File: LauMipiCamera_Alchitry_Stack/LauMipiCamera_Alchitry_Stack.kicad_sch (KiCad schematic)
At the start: 19 parts, among them J1 DF40C-50DP, J2 DF40C-80DP, J3 DF40C-80DP, SW1 SW_DIP_x4

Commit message: hw(mipi): import netlist onto the PCB; repair what F8 broke
Update PCB from Schematic pulled all 23 nets onto the board: 268 pads netted,
0 node mismatches against the schematic netlist, and kicad-cli reports
schematic_parity: 0. The scaffold's R_1206 became R_0402 and the 9 XAPP894
front-end resistors were added. KiCad also annotated the non-numeric refs
(R_SCL -> R_SCL1, J_CAM -> J_CAM1, R_LP* -> R_LP*1); schematic and PCB agree.

F8 ran with "replace footprints", which re-created every footprint with new
UUIDs at default placement. Two consequences, both fixed here:

1. J1/J2/J3 landed on F.Cu. They are bottom-side DF40 plugs, and their old
   coordinates encoded the Alchitry stack geometry -- Site B-A = 21.5 mm in x,
   Site B-C = 37.0 mm in y (ROADMAP SS3, from Br.step). Restored all three to
   B.Cu at their original positions, injecting the freshly computed pad nets
   into the pre-F8 footprint blocks. Geometry re-verified: 21.50 / 37.00 mm.

2. Twelve clearance errors appeared, all pad-to-pad *inside* a single
   connector. Both causes are settings that were written before the nets
   existed, so nothing had ever exercised them:
     * "MipiHS clearance to other nets" (0.25 mm, ~3W) applied to pads as well
       as tracks. DF40 is 0.4 mm pitch and the FFC 0.5 mm -- those gaps are
       fixed by the connector and can never satisfy it. Scoped to
       A.Type == 'Track'; track-vs-pad is still checked.
     * The MipiHS netclass clearance floor was 0.2 mm vs the DF40's actual
       0.17 mm pad gap. Lowered to 0.15 mm; 3W routing separation still comes
       from the custom rule.

DRC now: 0 copper violations, schematic_parity 0. The 47 remaining are all
silkscreen overlaps from the auto-placement, and 112 unconnected ratsnest items
because nothing is routed.

Next: place the parts (front-end resistors belong at J3, not the FFC -- SS3.4),
then recompute the placeholder track width/gap from the real stackup.

Co-Authored-By: Claude Opus 4.8 (1M context) <nore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
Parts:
- renumbered J_CAM to J_CAM1, R_LP0N to R_LP0N1, R_LP0P to R_LP0P1, R_LP1N to R_LP1N1, R_LP1P to R_LP1P1, R_LP2N to R_LP2N1, R_LP2P to R_LP2P1, R_SCL to R_SCL1, R_SDA to R_SDA1, R_TRIG to R_TRIG1
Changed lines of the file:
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@@
 		(in_pos_files yes)
 		(dnp no)
-		(property "Reference" "J_CAM"
+		(property "Reference" "J_CAM1"
 			(at 282.57 96.52 0)
 			(show_name no)
@@
 			(project "LauMipiCamera_Alchitry_Stack"
 				(path "/fcd4dd93-c3dd-49e9-b78a-67baf19f0e7c"
-					(reference "J_CAM")
+					(reference "J_CAM1")
 					(unit 1)
 				)
@@
 		(in_pos_files yes)
 		(dnp no)
-		(property "Reference" "R_LP0P"
+		(property "Reference" "R_LP0P1"
 			(at 213.11 68.58 0)
 			(show_name no)
@@
 			(project "LauMipiCamera_Alchitry_Stack"
 				(path "/fcd4dd93-c3dd-49e9-b78a-67baf19f0e7c"
-					(reference "R_LP0P")
+					(reference "R_LP0P1")
 					(unit 1)
 				)
@@
 		(in_pos_files yes)
 		(dnp no)
-		(property "Reference" "R_LP1P"
+		(property "Reference" "R_LP1P1"
 			(at 248.67 68.58 0)
 			(show_name no)
@@
 			(project "LauMipiCamera_Alchitry_Stack"
 				(path "/fcd4dd93-c3dd-49e9-b78a-67baf19f0e7c"
-					(reference "R_LP1P")
+					(reference "R_LP1P1")
 					(unit 1)
 				)
@@
 		(in_pos_files yes)
 		(dnp no)
-		(property "Reference" "R_LP2P"
+		(property "Reference" "R_LP2P1"
 			(at 284.23 68.58 0)
 			(show_name no)
@@
 			(project "LauMipiCamera_Alchitry_Stack"
 				(path "/fcd4dd93-c3dd-49e9-b78a-67baf19f0e7c"
-					(reference "R_LP2P")
+					(reference "R_LP2P1")
 					(unit 1)
 				)
@@
 		(in_pos_files yes)
 		(dnp no)
-		(property "Reference" "R_SDA"
+		(property "Reference" "R_SDA1"
 			(at 342.65 97.79 0)
 			(show_name no)
@@
 			(project "LauMipiCamera_Alchitry_Stack"
 				(path "/fcd4dd93-c3dd-49e9-b78a-67baf19f0e7c"
-					(reference "R_SDA")
+					(reference "R_SDA1")
 					(unit 1)
 				)
@@
 		(in_pos_files yes)
 		(dnp no)
-		(property "Reference" "R_LP0N"
+		(property "Reference" "R_LP0N1"
 			(at 230.89 68.58 0)
 			(show_name no)
@@
 			(project "LauMipiCamera_Alchitry_Stack"
 				(path "/fcd4dd93-c3dd-49e9-b78a-67baf19f0e7c"
-					(reference "R_LP0N")
+					(reference "R_LP0N1")
 					(unit 1)
 				)
@@
 		(in_pos_files yes)
 		(dnp no)
-		(property "Reference" "R_TRIG"
+		(property "Reference" "R_TRIG1"
 			(at 357.89 97.79 0)
 			(show_name no)
@@
 			(project "LauMipiCamera_Alchitry_Stack"
 				(path "/fcd4dd93-c3dd-49e9-b78a-67baf19f0e7c"
-					(reference "R_TRIG")
+					(reference "R_TRIG1")
 					(unit 1)
 				)
@@
 		(in_pos_files yes)
 		(dnp no)
-		(property "Reference" "R_LP1N"
+		(property "Reference" "R_LP1N1"
 			(at 266.45 68.58 0)
 			(show_name no)
@@
 			(project "LauMipiCamera_Alchitry_Stack"
 				(path "/fcd4dd93-c3dd-49e9-b78a-67baf19f0e7c"
-					(reference "R_LP1N")
+					(reference "R_LP1N1")
 					(unit 1)
 				)
@@
 		(in_pos_files yes)
 		(dnp no)
-		(property "Reference" "R_SCL"
+		(property "Reference" "R_SCL1"
 			(at 328.68 97.79 0)
 			(show_name no)
@@
 			(project "LauMipiCamera_Alchitry_Stack"
 				(path "/fcd4dd93-c3dd-49e9-b78a-67baf19f0e7c"
-					(reference "R_SCL")
+					(reference "R_SCL1")
 					(unit 1)
 				)
@@
 		(in_pos_files yes)
 		(dnp no)
-		(property "Reference" "R_LP2N"
+		(property "Reference" "R_LP2N1"
 			(at 302.01 68.58 0)
 			(show_name no)
@@
 			(project "LauMipiCamera_Alchitry_Stack"
 				(path "/fcd4dd93-c3dd-49e9-b78a-67baf19f0e7c"
-					(reference "R_LP2N")
-					(unit 1)
-				)
+					(reference "R_LP2N1")
+					(unit 1)
+				)

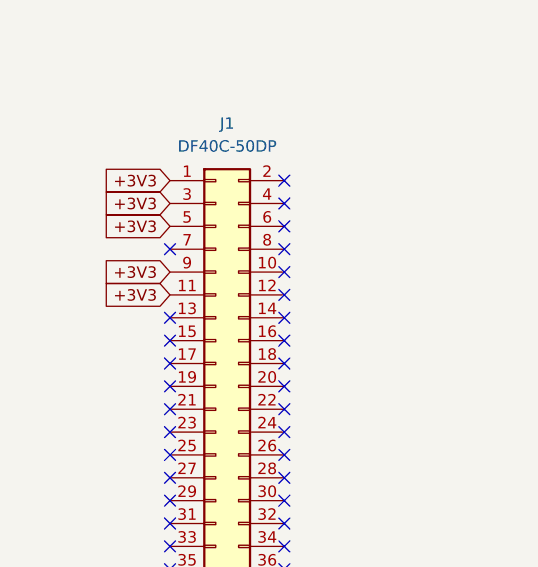
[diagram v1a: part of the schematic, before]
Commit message: hw(mipi): explicit GND returns for SW1 and C1/C2; trim J1 +3V3 to 3 contacts
GND ties (13 segments, 5 vias). Both loads now have a dedicated copper return to
a DF40 ground pin, rather than relying on the pour alone -- and they return to
DIFFERENT connectors, so the paths are genuinely separate:

  * SW1's four GND pads -> short F.Cu stubs west to a B.Cu spine at x=133.5,
    then east under the board to J3 pad 2 (GND, 149.745/100.057), entering from
    the north as even-row pads require.
    The spine cannot run at x=135.305 (through the pads) because SW_BLUE and
    SW_RED thread the gaps between those same GND pads at y=93.46 and y=99.0.
  * C1/C2 GND pads -> F.Cu around the caps' own +3V3 pads, east at y=71.5, then
    a via down into J2 pad 1 (GND, 149.745/65.767).

J1 +3V3: 1/3/5/9/11 -> 1/3/5.

  Hirose DF40 contacts are rated 0.3 A each. The camera draws ~260 mA, so ONE
  pin (the fabricated trigger board's choice) sits at 87% of rating with no
  headroom for inrush. Three contacts give 0.9 A, a 3.5x margin, and cut the
  contact-resistance drop.

  Five was the wrong trade. ROADMAP asserts "+3V3 is on Site A odd pins 1-13"
  but its own open-items list (SS208.3) flags that map as needing
  re-confirmation, and warns "never wire VCC" (the even pins). No Br schematic
  is in the repo. Every additional pin tied is another opportunity to short
  +3V3 to a different rail if that map is wrong, for current margin we do not
  need. Pins 9 and 11 are now no-connects in both schematic and PCB.

  STILL GATED: confirm Site A's pin map against the Br schematic before fab.
  If it turns out only pin 1 is +3V3, this is a short.

DRC: 0 copper violations, schematic_parity 0. ERC: 1 (the known cached
Conn_01x22 symbol). SW1 and C1/C2 have no ratsnest left. Ratsnest 102 -> 96.

Co-Authored-By: Claude Opus 4.8 (1M context) <noreply@anthropic.com>
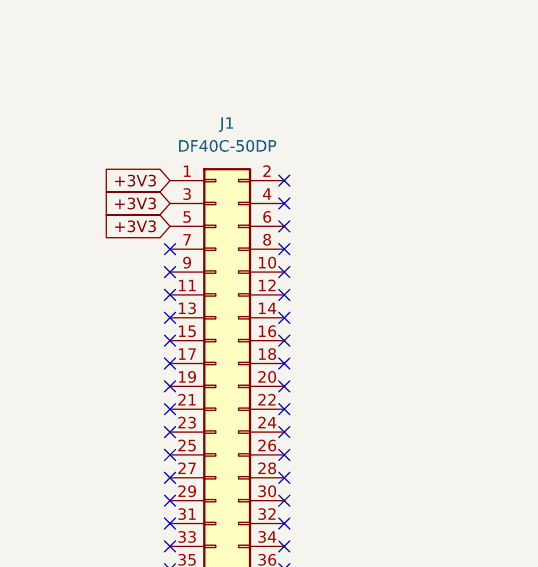
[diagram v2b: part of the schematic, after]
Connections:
- net +3V3: no longer J1.11 (Pin_11), J1.9 (Pin_9)
- no-connect marks 133 -> 135
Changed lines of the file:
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@@
 		)
 	)
-	(global_label "+3V3"
-		(shape input)
-		(at 90.17 181.61 180)
-		(effects
-			(font
-				(size 1.27 1.27)
-			)
-			(justify right)
-		)
-		(property "Intersheetrefs" "${INTERSHEET_REFS}"
-			(at 90.17 181.61 0)
-			(hide yes)
-			(show_name no)
-			(do_not_autoplace no)
-			(effects
-				(font
-					(size 1.27 1.27)
-				)
-			)
-		)
-	)
 	(global_label "GND"
 		(shape input)
@@
 		)
 	)
-	(global_label "+3V3"
-		(shape input)
-		(at 90.17 179.07 180)
-		(effects
-			(font
-				(size 1.27 1.27)
-			)
-			(justify right)
-		)
-		(property "Intersheetrefs" "${INTERSHEET_REFS}"
-			(at 90.17 179.07 0)
-			(hide yes)
-			(show_name no)
-			(do_not_autoplace no)
-			(effects
-				(font
-					(size 1.27 1.27)
-				)
-			)
-		)
-	)
 	(global_label "CAM_TRIG_R"
 		(shape input)
@@
 	)
 	(embedded_fonts no)
+	(no_connect
+		(at 90.17 181.61)
+	)
+	(no_connect
+		(at 90.17 179.07)
+	)
 )
